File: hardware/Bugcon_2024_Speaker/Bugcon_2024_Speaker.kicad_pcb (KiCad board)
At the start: 2 copper layers, 81.7 x 139.8 mm, 49 parts, among them J1 OLED, J2 Add_On, J4 Battery, J5 Battery, P1 USB_C_Plug_USB2.0, Q1 DMG3415U-7, SW1 ON, U1 ESP32-C6-WROOM-1U-N4, U2 AP2112K-3.3

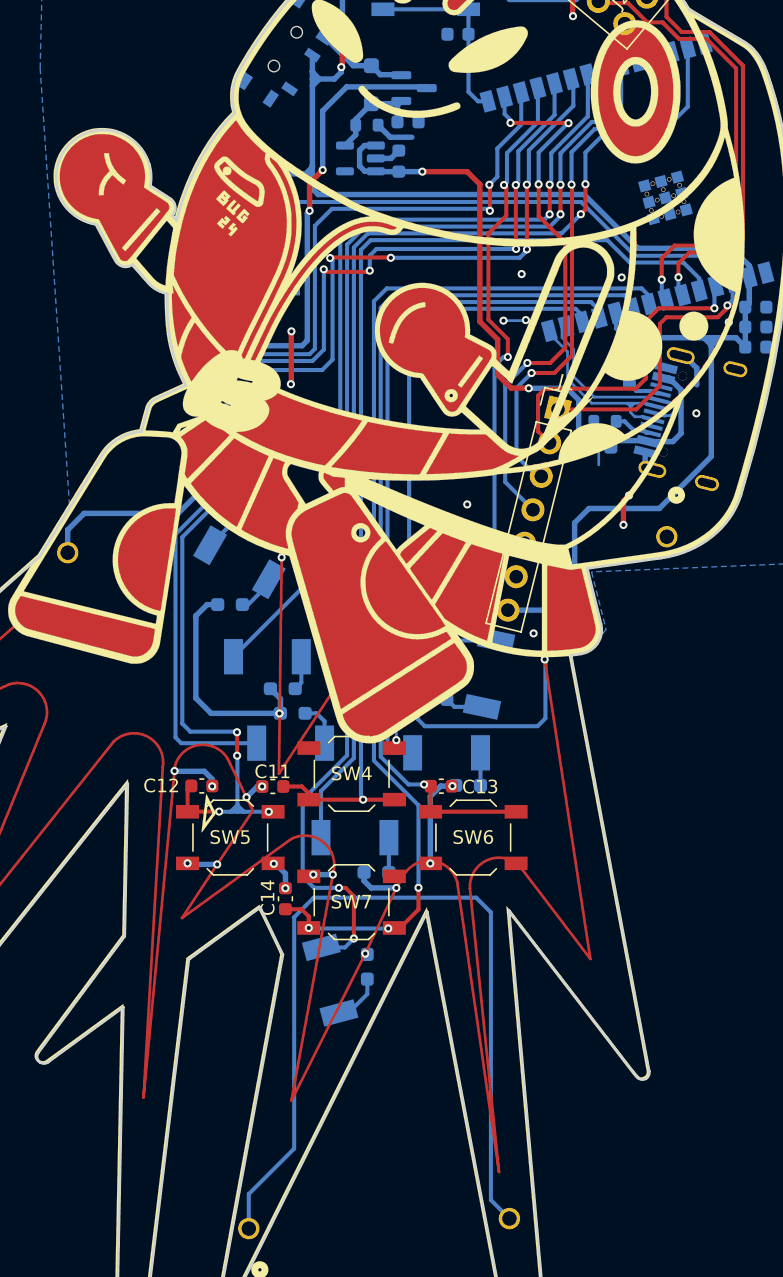
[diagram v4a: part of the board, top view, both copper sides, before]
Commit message: feat(Hw): Change LEDs
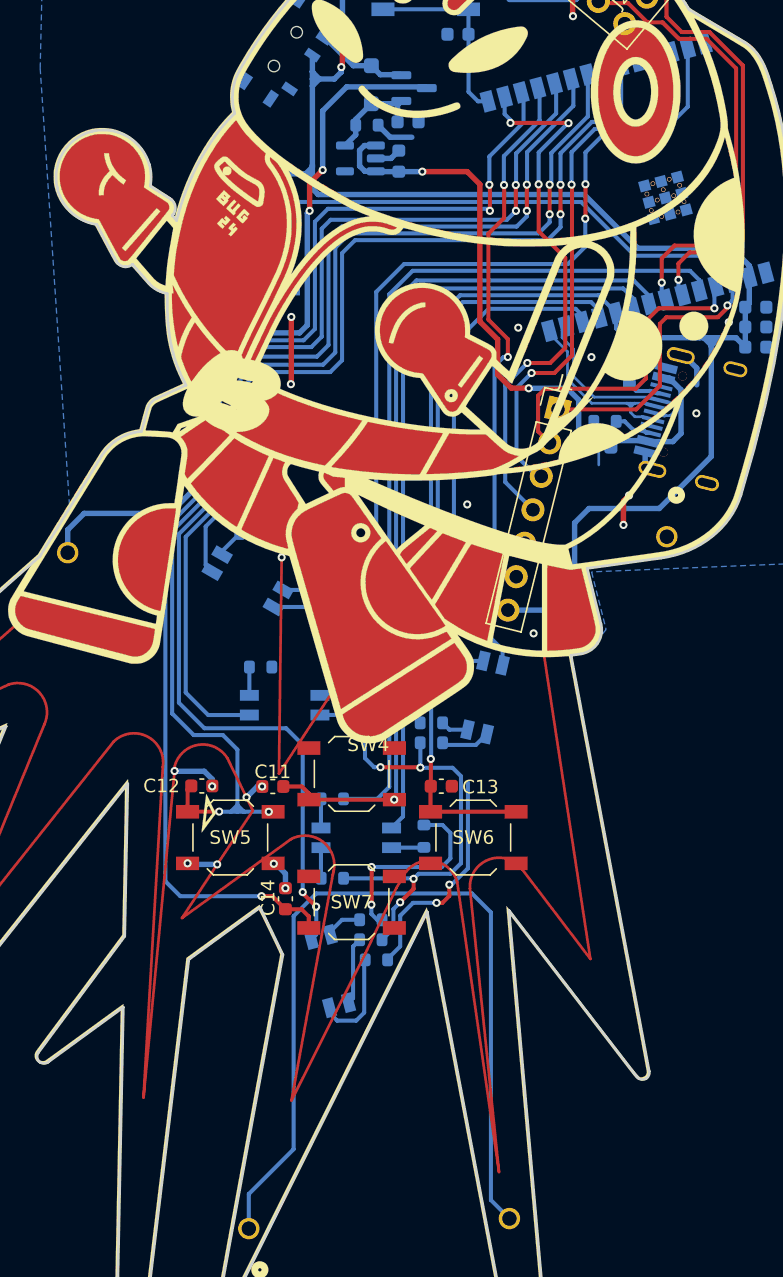
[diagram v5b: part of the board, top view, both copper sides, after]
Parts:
- removed D6, D7: Y_LED, Library:LYT77K-K2M1
- removed D9: R_LED, Library:LYT77K-K2M1
- added D8: LED_RABG, Library:AAA3528SURKCGKC09, B.Cu at (118.7, 97.4)
- added R14: 330, Resistor_SMD:R_0603_1608Metric, B.Cu at (125.0, 98.6)
- added R15: 330, Resistor_SMD:R_0603_1608Metric, B.Cu at (118.9, 93.9)
- added R16: 330, Resistor_SMD:R_0603_1608Metric, B.Cu at (132.2, 109.3)
- added R17: 330, Resistor_SMD:R_0603_1608Metric, B.Cu at (134.7, 100.6)
- added R18: 330, Resistor_SMD:R_0603_1608Metric, B.Cu at (128.2, 125.3)
- added R19: 330, Resistor_SMD:R_0603_1608Metric, B.Cu at (127.8, 123.9)
- added R20: 330, Resistor_SMD:R_0603_1608Metric, B.Cu at (127.8, 122.4)
- added R9: 330, Resistor_SMD:R_0603_1608Metric, B.Cu at (125.0, 100.1)
- D2, D3, D4, D5: value R_LED -> LED_RABG; footprint Library:LYT77K-K2M1 -> Library:AAA3528SURKCGKC09
- R10, R11, R12, R13, R5, R7, R8: value 220 -> 330; footprint Resistor_SMD:R_0603_1608Metric_Pad0.98x0.95mm_HandSolder -> Resistor_SMD:R_0603_1608Metric
- U2: value AP2112K-3.3 -> XC6220B331MR-G
- moved D4 23.7 mm to (136.2, 106.0), turned to -103 degrees
- moved R11 12.1 mm to (124.9, 119.3)
- moved R13 11.7 mm to (132.2, 107.9), turned to 0 degrees
- moved R12 10.5 mm to (131.7, 116.2), turned to -90 degrees
- moved D5 10.00 mm to (124.8, 126.2), turned to -75 degrees
- moved D3 9.14 mm to (126.7, 116.3)
- moved R10 8.89 mm to (124.9, 113.5)
- moved R7 6.07 mm to (127.3, 105.8), turned to 180 degrees
- moved R5 5.33 mm to (127.3, 107.3)
- moved R8 5.12 mm to (119.7, 103.8)
- moved D2 2.83 mm to (121.4, 106.6), turned to 0 degrees
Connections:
- D2 pad 1: Net-(D2-K) -> Net-(D2-RK)
- D2 pad 2: /LED4 -> /COM2
- D3 pad 1: Net-(D3-K) -> Net-(D3-RK)
- D3 pad 2: /LED5 -> /COM3
- D4 pad 1: Net-(D4-K) -> Net-(D4-RK)
- D4 pad 2: /LED6 -> /COM4
- D5 pad 1: Net-(D5-K) -> Net-(D5-RK)
- D5 pad 2: /LED7 -> /COM5
- R1 pad 1: Net-(U1-IO8) -> /RIGHT
- R10 pad 1: Net-(D9-K) -> /LED1
- R10 pad 2: GND -> Net-(D3-RK)
- R11 pad 1: Net-(D3-K) -> /LED2
- R11 pad 2: GND -> Net-(D3-GK)
- R12 pad 1: Net-(D4-K) -> /LED3
- R12 pad 2: GND -> Net-(D3-BK)
- R13 pad 1: Net-(D5-K) -> /LED1
- R13 pad 2: GND -> Net-(D4-RK)
- R5 pad 1: Net-(D2-K) -> /LED1
- R5 pad 2: GND -> Net-(D2-RK)
- R7 pad 1: Net-(D6-K) -> /LED2
- R7 pad 2: GND -> Net-(D2-GK)
- R8 pad 1: Net-(D7-K) -> /LED3
- R8 pad 2: GND -> Net-(D2-BK)
- U1 pad 10: Net-(U1-IO8) -> /RIGHT
- U1 pad 11: /LED5 -> /COM4
- U1 pad 12: /LED1 -> /LED3
- U1 pad 17: /LED4 -> /DOWN
- U1 pad 20: /LED2 -> /COM5
- U1 pad 21: /LED3 -> /COM2
- U1 pad 23: /LED6 -> /COM1
- U1 pad 27: /LED7 -> /LED2
- U1 pad 5: /UP -> /LED1
- U1 pad 8: /DOWN -> /UP
- U1 pad 9: /RIGHT -> /COM3
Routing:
- net /COM5: track 0.00 -> 93.9 mm, vias 0 -> 4
- net /LED6: track 88.5 -> 0.00 mm, vias 4 -> 0
- net /LED7: track 80.2 -> 0.00 mm, vias 2 -> 0
- net /LED4: track 74.9 -> 0.00 mm, vias 2 -> 0
- net /COM2: track 0.00 -> 74.4 mm, vias 0 -> 2
- net /COM1: track 0.00 -> 62.5 mm, vias 0 -> 2
- net /COM3: track 0.00 -> 57.3 mm
- net /LED5: track 50.7 -> 0.00 mm
- net /LED2: track 57.4 -> 106.8 mm, vias 4 -> 6
- net GND: track 350.2 -> 301.3 mm, vias 31 -> 20
- net /LED1: track 42.9 -> 88.3 mm, vias 0 -> 2
- net /COM4: track 0.00 -> 40.8 mm
- net /LED3: track 61.6 -> 46.4 mm
- net /DOWN: track 79.1 -> 91.8 mm
- net /UP: track 76.6 -> 66.0 mm
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
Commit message: feat(Hw):Update_Route
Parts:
- moved R15 2.27 mm to (121.2, 94.3)
- moved R20 0.43 mm to (127.8, 122.0)
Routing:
- net /LED3: track 46.4 -> 94.6 mm, vias 2 -> 6
- net /LED1: track 88.3 -> 108.4 mm, vias 2 -> 5
- net GND: track 301.3 -> 315.0 mm, vias 20 -> 27
- net /DOWN: track 91.8 -> 99.2 mm, vias 3 -> 5
- net Net-(D8-BK): track 2.10 -> 4.05 mm
- net /LED2: track 106.8 -> 107.3 mm
- net /SDAO: track 40.3 -> 40.8 mm
- net Net-(D5-BK): track 2.73 -> 3.19 mm, vias 0 -> 2
- net /LEFT: vias 4 -> 6

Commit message: feat(Hw):Update_Route
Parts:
- moved R10 0.96 mm to (125.7, 112.8)
- moved R9 0.61 mm to (125.0, 100.7)
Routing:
- net /LED3: track 94.6 -> 108.8 mm, vias 6 -> 9
- net /LED1: track 108.4 -> 105.7 mm, vias 5 -> 6
- net Net-(D3-RK): track 2.15 -> 3.08 mm

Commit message: feat: add labels and logos
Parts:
- added G***: LOGO, Aesthetics:electronic_cats_logo_8x6, B.Cu at (128.9, 73.2)
- added kibuzzard-66F1E442: G***, kibuzzard-66F1E442, B.Cu at (125.0, 54.1)
- added kibuzzard-66F1E44B: G***, kibuzzard-66F1E44B, B.Cu at (120.3, 63.6)
- added kibuzzard-66F1E456: G***, kibuzzard-66F1E456, B.Cu at (118.3, 78.2)
- added kibuzzard-66F1E462: G***, kibuzzard-66F1E462, B.Cu at (138.6, 56.7)
